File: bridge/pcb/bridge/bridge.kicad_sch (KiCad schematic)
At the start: 17 parts, among them J1 Screw_Terminal_01x06, J10 12V_Enable, J2 Screw_Terminal_01x06, J3 Screw_Terminal_01x06, J4 Conn_01x23, SW1 SW_SPST, U2 J104D2C12VDC.20S

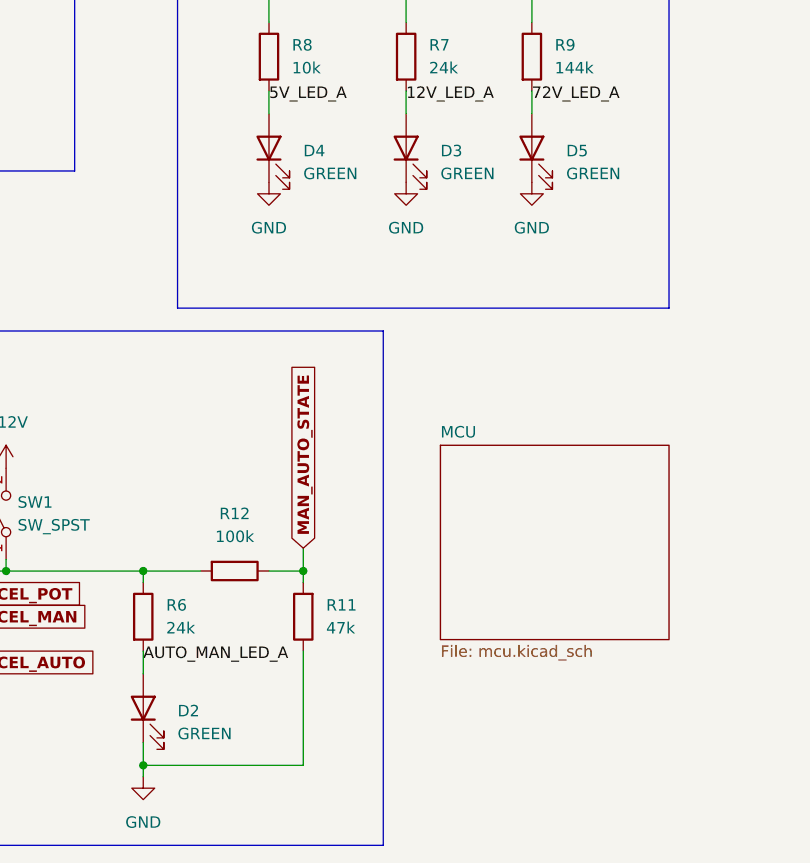
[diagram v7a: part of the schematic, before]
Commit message: Added status LED's for all of the motor controller switches
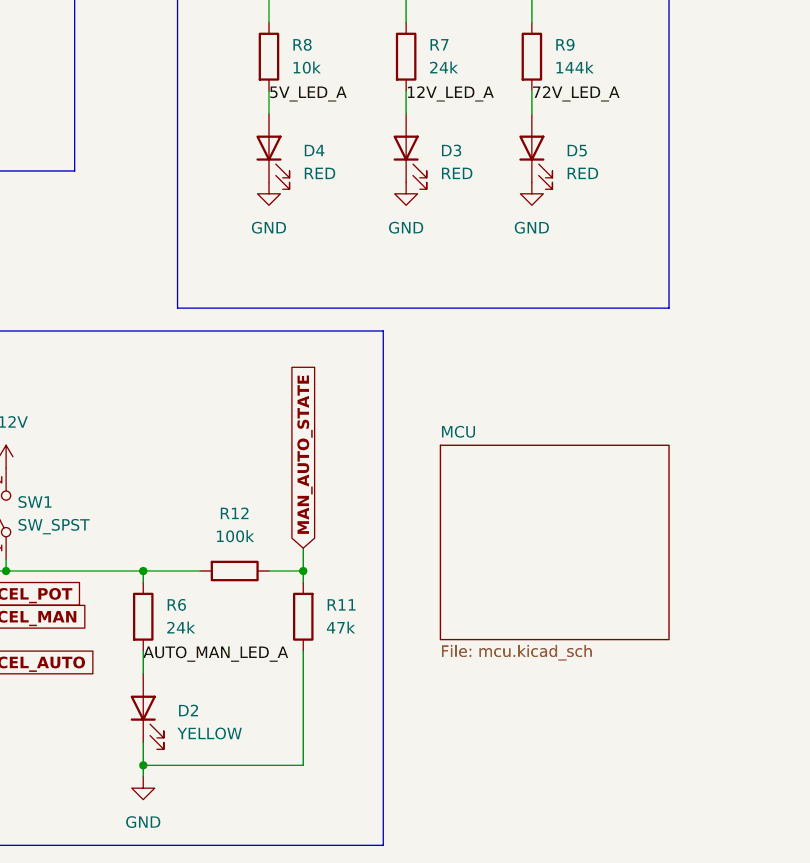
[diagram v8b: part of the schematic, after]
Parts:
- D2: value GREEN -> YELLOW
- D3, D4, D5: value GREEN -> RED
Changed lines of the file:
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@@
       (effects (font (size 1.27 1.27)) (justify right))
     )
-    (property "Value" "GREEN" (at 114.3 162.8775 90)
+    (property "Value" "YELLOW" (at 114.3 162.8775 90)
       (effects (font (size 1.27 1.27)) (justify right))
     )
@@
       (effects (font (size 1.27 1.27)) (justify right))
     )
-    (property "Value" "GREEN" (at 128.27 100.6475 90)
+    (property "Value" "RED" (at 128.27 100.6475 90)
       (effects (font (size 1.27 1.27)) (justify right))
     )
@@
       (effects (font (size 1.27 1.27)) (justify right))
     )
-    (property "Value" "GREEN" (at 157.48 100.6475 90)
+    (property "Value" "RED" (at 157.48 100.6475 90)
       (effects (font (size 1.27 1.27)) (justify right))
     )
@@
       (effects (font (size 1.27 1.27)) (justify right))
     )
-    (property "Value" "GREEN" (at 143.51 100.6475 90)
-      (effects (font (size 1.27 1.27)) (justify right))
-    )
+    (property "Value" "RED" (at 143.51 100.6475 90)
+      (effects (font (size 1.27 1.27)) (justify right))
+    )
